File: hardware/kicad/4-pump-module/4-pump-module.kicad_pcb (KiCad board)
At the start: 2 copper layers, 85.5 x 21 mm, 30 parts, among them J1 Conn_02x03_Counter_Clockwise, J10 Pololu2-PWR, J3 PUMP 1, J4 PUMP 2, J5 PUMP 3, J6 PUMP 4, J7 Pololu1-CTRL, J8 Pololu1-PWR, J9 Pololu2-CTRL, U1 MCP23017x-x-SO

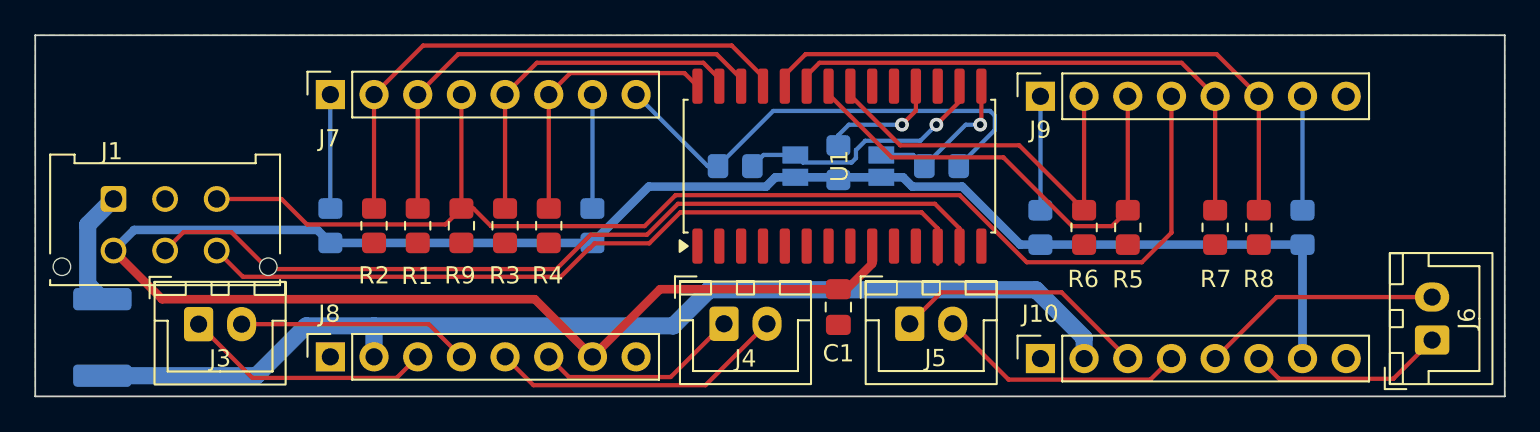
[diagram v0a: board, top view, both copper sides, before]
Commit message: Lock in both PCBs for fab and sync hardware, firmware pins, and procurement.
4-pump and main-controller KiCad layouts are ordered; motherboard GPIO map, CAD refs, bench logs, and AliExpress/OSH Park procurement notes are brought current so assembly can proceed when boards arrive.

Co-authored-by: Cursor <cursoragent@cursor.com>
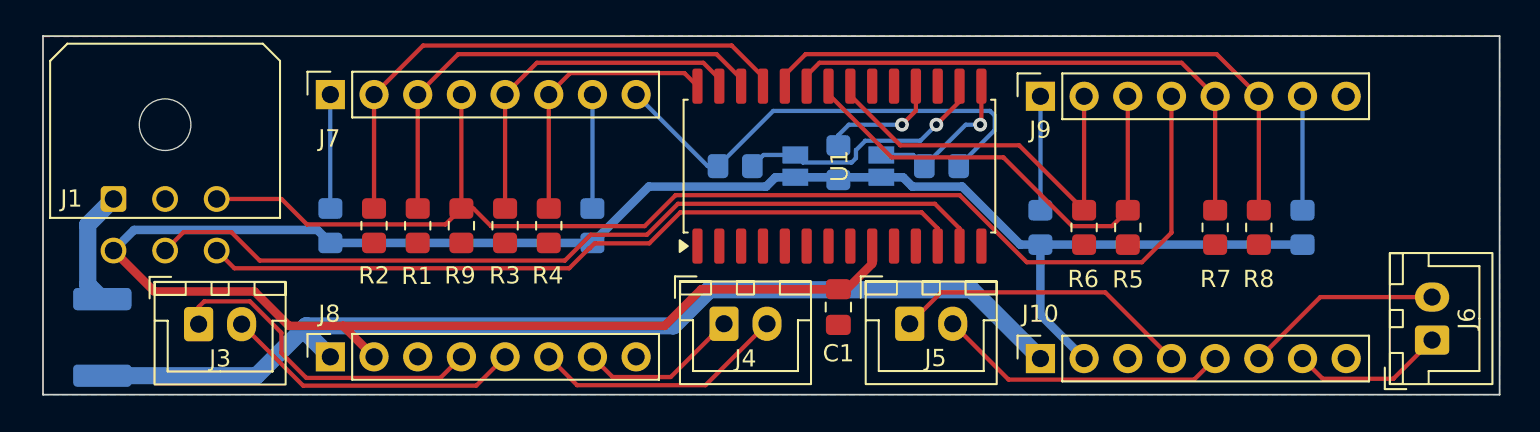
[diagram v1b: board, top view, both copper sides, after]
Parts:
- J1: footprint Connector_Molex:Molex_Micro-Fit_3.0_43045-0612_2x03_P3.00mm_Vertical -> Connector_Molex:Molex_Micro-Fit_3.0_43045-0600_2x03_P3.00mm_Horizontal
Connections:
- J10 pad 1: GND -> /VMOT
- J10 pad 2: /VMOT -> +3V3
- J10 pad 3: /P3_M+ -> GND
- J10 pad 4: /P3_M- -> /P3_M+
- J10 pad 5: /P4_M- -> /P3_M-
- J10 pad 6: /P4_M+ -> /P4_M-
- J10 pad 7: +3V3 -> /P4_M+
- J8 pad 1: GND -> /VMOT
- J8 pad 2: /VMOT -> +3V3
- J8 pad 3: /P1_M+ -> GND
- J8 pad 4: /P1_M- -> /P1_M+
- J8 pad 5: /P2_M- -> /P1_M-
- J8 pad 6: /P2_M+ -> /P2_M-
- J8 pad 7: +3V3 -> /P2_M+
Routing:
- net /P1_M+: track 14.5 -> 19.5 mm
- net /P1_M-: track 13.6 -> 17.5 mm
- net /VMOT: track 63.3 -> 60.7 mm
- net /P4_M+: track 11.5 -> 8.95 mm
- net /P2_M+: track 12.0 -> 9.42 mm
- net /P3_M+: track 15.0 -> 17.6 mm
- net /P2_M-: track 17.4 -> 14.9 mm
- net /P4_M-: track 14.1 -> 11.6 mm
- net /P3_M-: track 14.6 -> 17.1 mm
- net +3V3: track 130.2 -> 132.0 mm
- net /SDA: track 51.7 -> 50.3 mm
- net /SCL: track 46.5 -> 45.1 mm
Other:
- board size 85.5 x 21 mm -> 84.7 x 20.9 mm
- board text added: "Rumtime 4-Pump Board v1.0 Chris Lawson"
- board text added: "try { pourRum(); } catch RumtimeException { pourRumHarder(); }"
